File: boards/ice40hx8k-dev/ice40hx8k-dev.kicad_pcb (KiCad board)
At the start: 6 copper layers, 50 x 50 mm, 52 parts, among them U1 ICE40HX8K-CT256

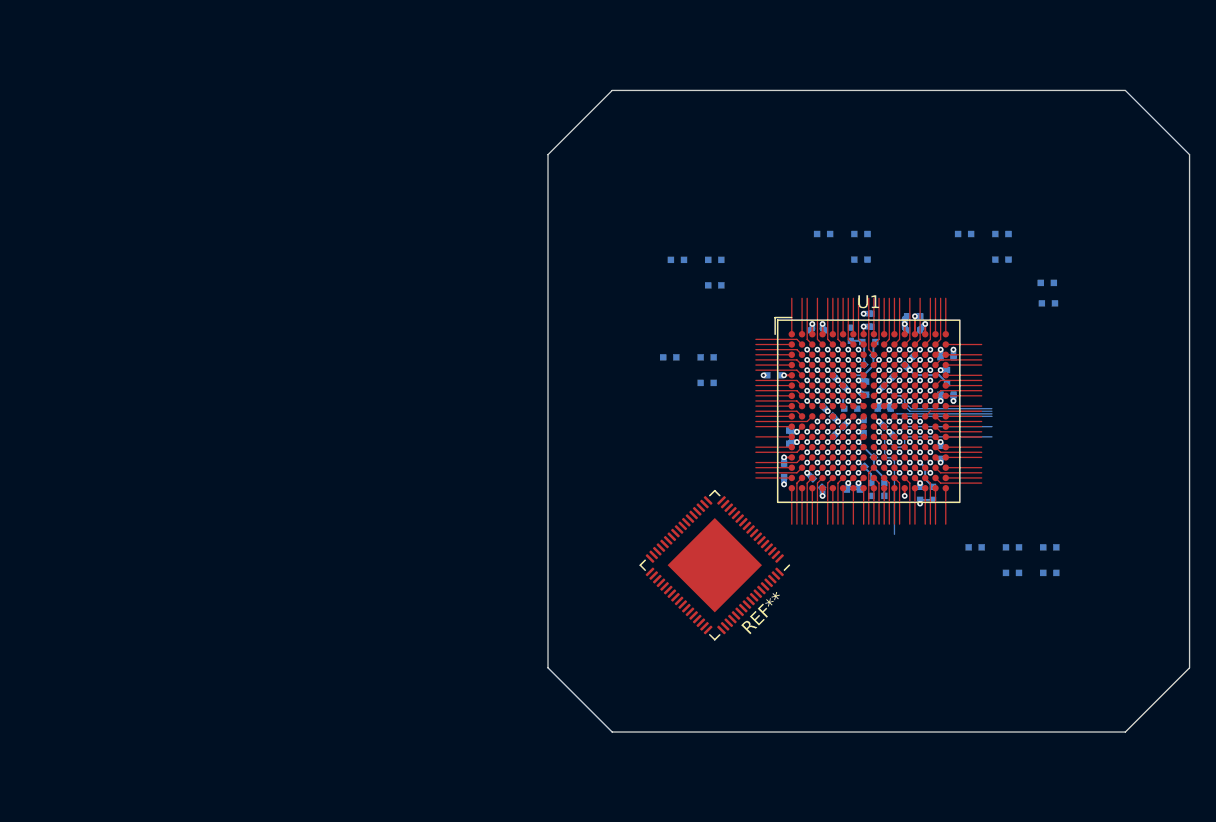
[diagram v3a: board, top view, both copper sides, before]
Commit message: Add USB connector and FT2323 symbol.
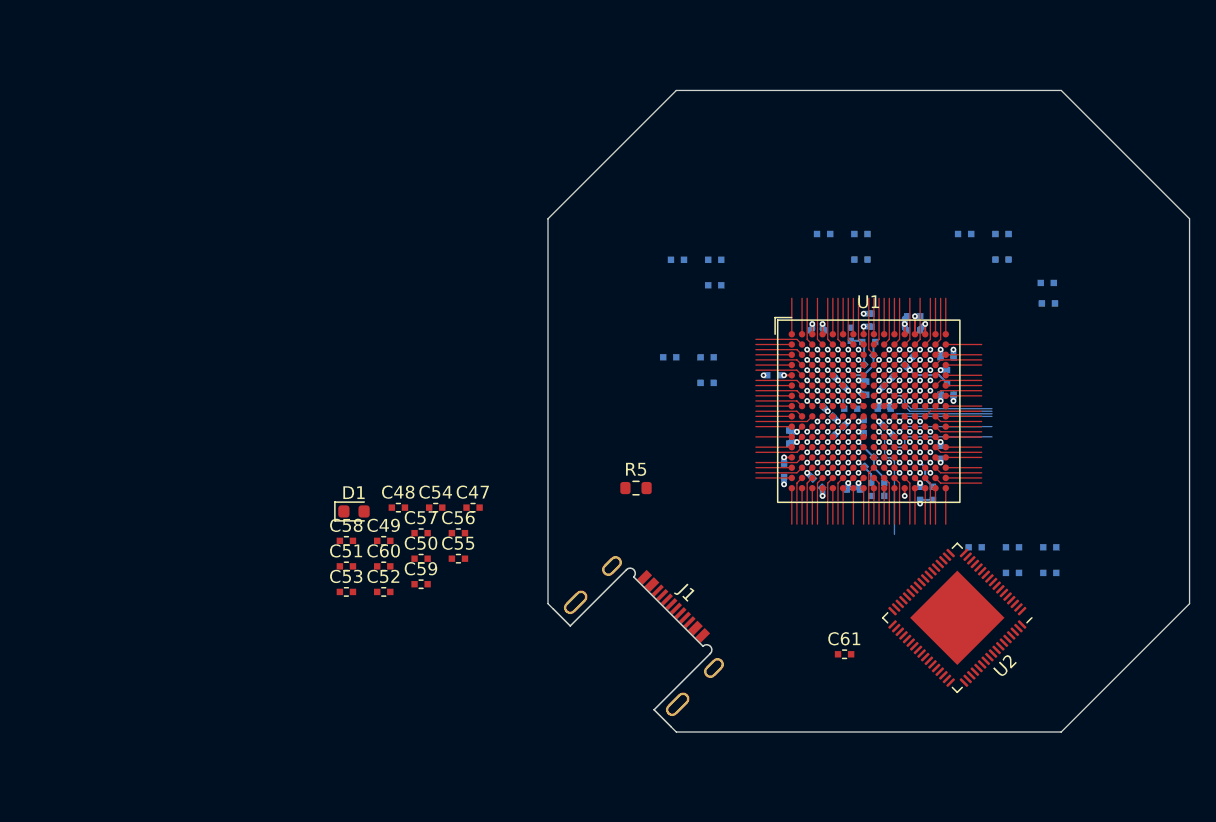
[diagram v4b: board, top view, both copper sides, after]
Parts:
- added C47: 10u, 0Local:C_SMD_0402_Pad0.5mm, F.Cu at (114.2, 102.5)
- added C48: 100n, 0Local:C_SMD_0402_Pad0.5mm, F.Cu at (108.3, 102.5)
- added C49: 100n, 0Local:C_SMD_0402_Pad0.5mm, F.Cu at (107.2, 105.1)
- added C50: 100n, 0Local:C_SMD_0402_Pad0.5mm, F.Cu at (110.1, 106.5)
- added C51: 100n, 0Local:C_SMD_0402_Pad0.5mm, F.Cu at (104.3, 107.1)
- added C52: 100n, 0Local:C_SMD_0402_Pad0.5mm, F.Cu at (107.2, 109.1)
- added C53: 100n, 0Local:C_SMD_0402_Pad0.5mm, F.Cu at (104.3, 109.1)
- added C54: 100n, 0Local:C_SMD_0402_Pad0.5mm, F.Cu at (111.2, 102.5)
- added C55: 100n, 0Local:C_SMD_0402_Pad0.5mm, F.Cu at (113.0, 106.5)
- added C56: 100n, 0Local:C_SMD_0402_Pad0.5mm, F.Cu at (113.0, 104.5)
- added C57: 100n, 0Local:C_SMD_0402_Pad0.5mm, F.Cu at (110.1, 104.5)
- added C58: 100n, 0Local:C_SMD_0402_Pad0.5mm, F.Cu at (104.3, 105.1)
- added C59: 100n, 0Local:C_SMD_0402_Pad0.5mm, F.Cu at (110.1, 108.5)
- added C60: 100n, 0Local:C_SMD_0402_Pad0.5mm, F.Cu at (107.2, 107.1)
- added C61: 100n, 0Local:C_SMD_0402_Pad0.5mm, F.Cu at (143.1, 113.9)
- added D1: D_Schottky, Diode_SMD:D_0603_1608Metric, F.Cu at (104.9, 102.8)
- added J1: USB4500-03-0-A, 0Local:GCT_USB4500, F.Cu at (126.9, 113.1)
- added R5: 12k, Resistor_SMD:R_0603_1608Metric, F.Cu at (126.9, 101.0)
- moved U2 19.3 mm to (151.9, 111.1)
- renumbered REF** to U2
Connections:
- U2 pad 1: (no net) -> unconnected-(U2-Pad1)
- U2 pad 10: (no net) -> +3V3
- U2 pad 11: (no net) -> /IO_Bank_2/ADBUS2
- U2 pad 12: (no net) -> /IO_Bank_2/ADBUS3
- U2 pad 13: (no net) -> /IO_Bank_2/ADBUS4
- U2 pad 14: (no net) -> /IO_Bank_2/ADBUS5
- U2 pad 15: (no net) -> /IO_Bank_2/ADBUS6
- U2 pad 16: (no net) -> /IO_Bank_2/ADBUS7
- U2 pad 17: (no net) -> /IO_Bank_2/ACBUS0
- U2 pad 18: (no net) -> /IO_Bank_2/ACBUS1
- U2 pad 19: (no net) -> /IO_Bank_2/ACBUS2
- U2 pad 2: (no net) -> unconnected-(U2-Pad2)
- U2 pad 20: (no net) -> /IO_Bank_2/ACBUS3
- U2 pad 21: (no net) -> /IO_Bank_2/ACBUS4
- U2 pad 22: (no net) -> /IO_Bank_2/ACBUS5
- U2 pad 23: (no net) -> /IO_Bank_2/ACBUS6
- U2 pad 24: (no net) -> /IO_Bank_2/ACBUS7
- U2 pad 25: (no net) -> Net-(U2-Pad25)
- U2 pad 26: (no net) -> +3V3
- U2 pad 27: (no net) -> unconnected-(U2-Pad27)
- U2 pad 28: (no net) -> unconnected-(U2-Pad28)
- U2 pad 29: (no net) -> GND
- U2 pad 3: (no net) -> GND
- U2 pad 30: (no net) -> Net-(U2-Pad30)
- U2 pad 31: (no net) -> Net-(U2-Pad25)
- U2 pad 32: (no net) -> unconnected-(U2-Pad32)
- U2 pad 33: (no net) -> unconnected-(U2-Pad33)
- U2 pad 34: (no net) -> /IO_Bank_2/BDBUS0
- U2 pad 35: (no net) -> /IO_Bank_2/BDBUS1
- U2 pad 36: (no net) -> /IO_Bank_2/BDBUS2
- U2 pad 37: (no net) -> /IO_Bank_2/BDBUS3
- U2 pad 38: (no net) -> /IO_Bank_2/BDBUS4
- U2 pad 39: (no net) -> +3V3
- U2 pad 4: (no net) -> unconnected-(U2-Pad4)
- U2 pad 40: (no net) -> /IO_Bank_2/BDBUS5
- U2 pad 41: (no net) -> /IO_Bank_2/BDBUS6
- U2 pad 42: (no net) -> /IO_Bank_2/BDBUS7
- U2 pad 43: (no net) -> unconnected-(U2-Pad43)
- U2 pad 44: (no net) -> Net-(U2-Pad25)
- U2 pad 45: (no net) -> /IO_Bank_2/BCBUS0
- U2 pad 46: (no net) -> /IO_Bank_2/BCBUS1
- U2 pad 47: (no net) -> /IO_Bank_2/BCBUS2
- U2 pad 48: (no net) -> /IO_Bank_2/BCBUS3
- U2 pad 49: (no net) -> /IO_Bank_2/BCBUS4
- U2 pad 5: (no net) -> unconnected-(U2-Pad5)
- U2 pad 50: (no net) -> /IO_Bank_2/BCBUS5
- U2 pad 51: (no net) -> +3V3
- U2 pad 52: (no net) -> /IO_Bank_2/BCBUS6
- U2 pad 53: (no net) -> /IO_Bank_2/BCBUS7
- U2 pad 54: (no net) -> unconnected-(U2-Pad54)
- U2 pad 55: (no net) -> unconnected-(U2-Pad55)
- U2 pad 56: (no net) -> unconnected-(U2-Pad56)
- U2 pad 57: (no net) -> Net-(U2-Pad57)
- U2 pad 58: (no net) -> /USB_Config/USB_D_N
- U2 pad 59: (no net) -> /USB_Config/USB_D_P
- U2 pad 6: (no net) -> /IO_Bank_2/ADBUS0
- U2 pad 60: (no net) -> Net-(R5-Pad1)
- U2 pad 61: (no net) -> Net-(U2-Pad61)
- U2 pad 62: (no net) -> /USB_Config/USB_CC2
- U2 pad 63: (no net) -> Net-(U2-Pad63)
- U2 pad 64: (no net) -> Net-(U2-Pad64)
- U2 pad 65: (no net) -> /USB_Config/USB_CC1
- U2 pad 66: (no net) -> Net-(U2-Pad25)
- U2 pad 67: (no net) -> unconnected-(U2-Pad67)
- U2 pad 68: (no net) -> unconnected-(U2-Pad68)
- U2 pad 7: (no net) -> /IO_Bank_2/ADBUS1
- U2 pad 8: (no net) -> Net-(U2-Pad25)
- U2 pad 9: (no net) -> GND
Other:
- outline, holes or cut-outs redrawn

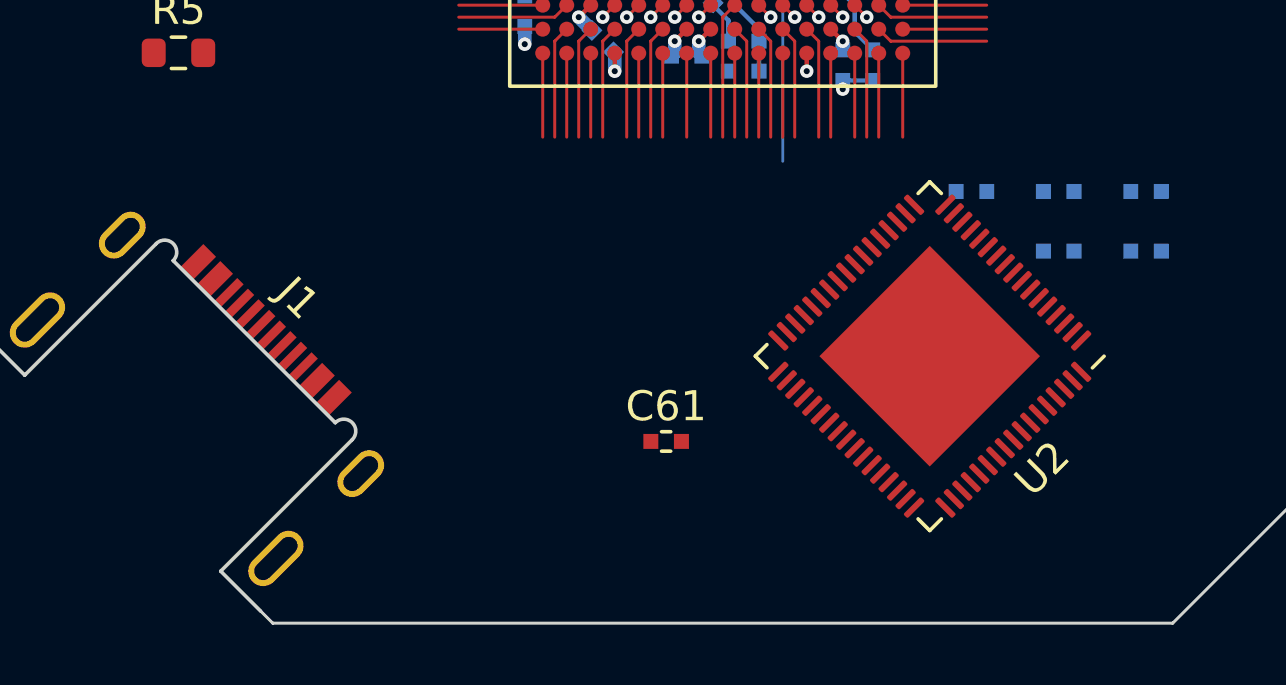
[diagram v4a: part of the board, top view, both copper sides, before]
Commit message: Use a lower-profile version of the USB connector.
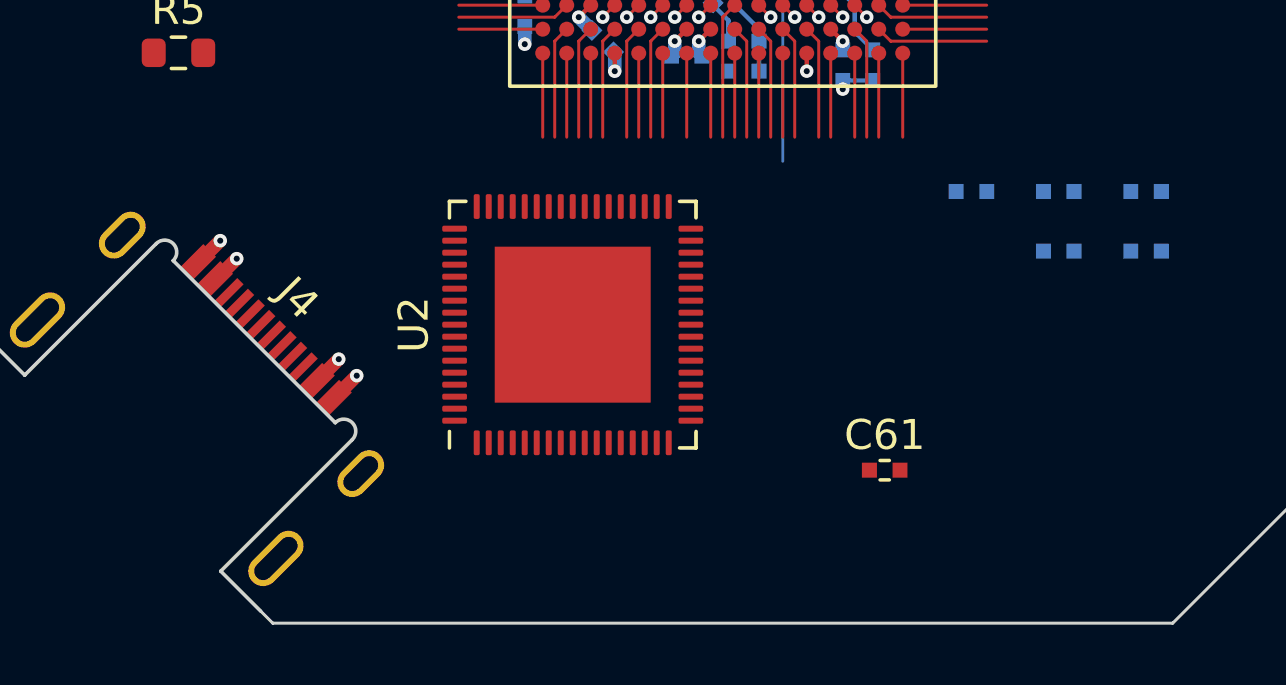
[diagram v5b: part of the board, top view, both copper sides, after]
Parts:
- J4: renamed from J1; value USB4500-03-0-A -> USB4520-03-1; footprint 0Local:GCT_USB4500 -> 0Local:GCT_USB45xx
- moved U2 11.9 mm to (140.0, 110.0), turned to 90 degrees
- moved C61 7.35 mm to (150.4, 114.9)
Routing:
- net GND: track 24.2 -> 26.3 mm, vias 26 -> 28
- net VBUS: track 0.00 -> 2.04 mm, vias 0 -> 2

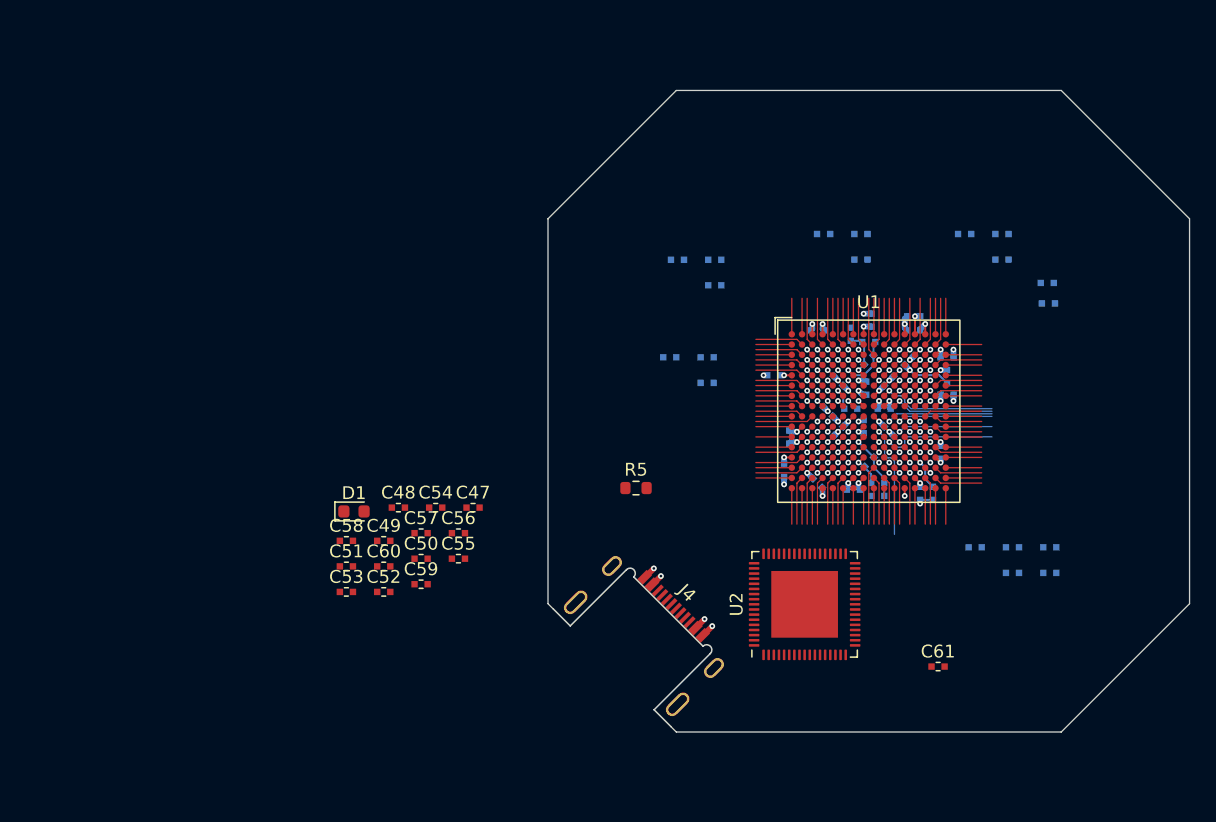
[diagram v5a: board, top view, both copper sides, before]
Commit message: Add Hirose connectors and standoffs.
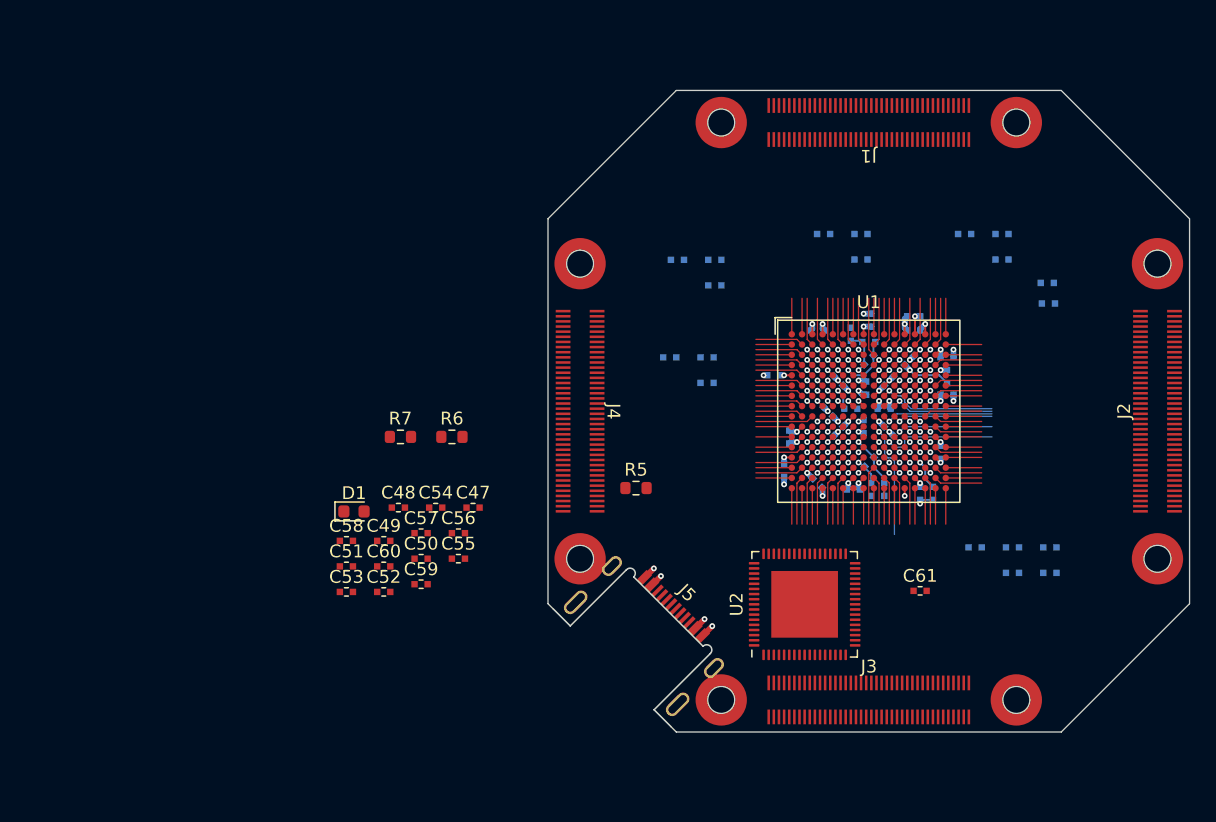
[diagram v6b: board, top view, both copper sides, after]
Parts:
- added H1: 9774020633, Mounting_Wuerth:Mounting_Wuerth_WA-SMSI-M1.6_H2mm_9774020633, F.Cu at (156.5, 72.5)
- added H2: 9774020633, Mounting_Wuerth:Mounting_Wuerth_WA-SMSI-M1.6_H2mm_9774020633, F.Cu at (133.5, 72.5)
- added H3: 9774020633, Mounting_Wuerth:Mounting_Wuerth_WA-SMSI-M1.6_H2mm_9774020633, F.Cu at (167.5, 106.5)
- added H4: 9774020633, Mounting_Wuerth:Mounting_Wuerth_WA-SMSI-M1.6_H2mm_9774020633, F.Cu at (167.5, 83.5)
- added H5: 9774020633, Mounting_Wuerth:Mounting_Wuerth_WA-SMSI-M1.6_H2mm_9774020633, F.Cu at (133.5, 117.5)
- added H6: 9774020633, Mounting_Wuerth:Mounting_Wuerth_WA-SMSI-M1.6_H2mm_9774020633, F.Cu at (156.5, 117.5)
- added H7: 9774020633, Mounting_Wuerth:Mounting_Wuerth_WA-SMSI-M1.6_H2mm_9774020633, F.Cu at (122.5, 83.5)
- added H8: 9774020633, Mounting_Wuerth:Mounting_Wuerth_WA-SMSI-M1.6_H2mm_9774020633, F.Cu at (122.5, 106.5)
- added J1: DF40HC(2.0)-80DS, 0Local:Hirose_DF40C-80DS, F.Cu at (145.0, 72.5)
- added J2: DF40HC(2.0)-80DS, 0Local:Hirose_DF40C-80DS, F.Cu at (167.5, 95.0)
- added J3: DF40HC(2.0)-80DS, 0Local:Hirose_DF40C-80DS, F.Cu at (145.0, 117.5)
- added J4: DF40HC(2.0)-80DS, 0Local:Hirose_DF40C-80DS, F.Cu at (122.5, 95.0)
- added R6: 100k, Resistor_SMD:R_0603_1608Metric, F.Cu at (112.5, 97.0)
- added R7: 15k, Resistor_SMD:R_0603_1608Metric, F.Cu at (108.5, 97.0)
- moved C61 6.06 mm to (149.0, 109.0)
- renumbered J4 to J5

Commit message: Switch to 4mm Hirose connectors and different mounting holes.
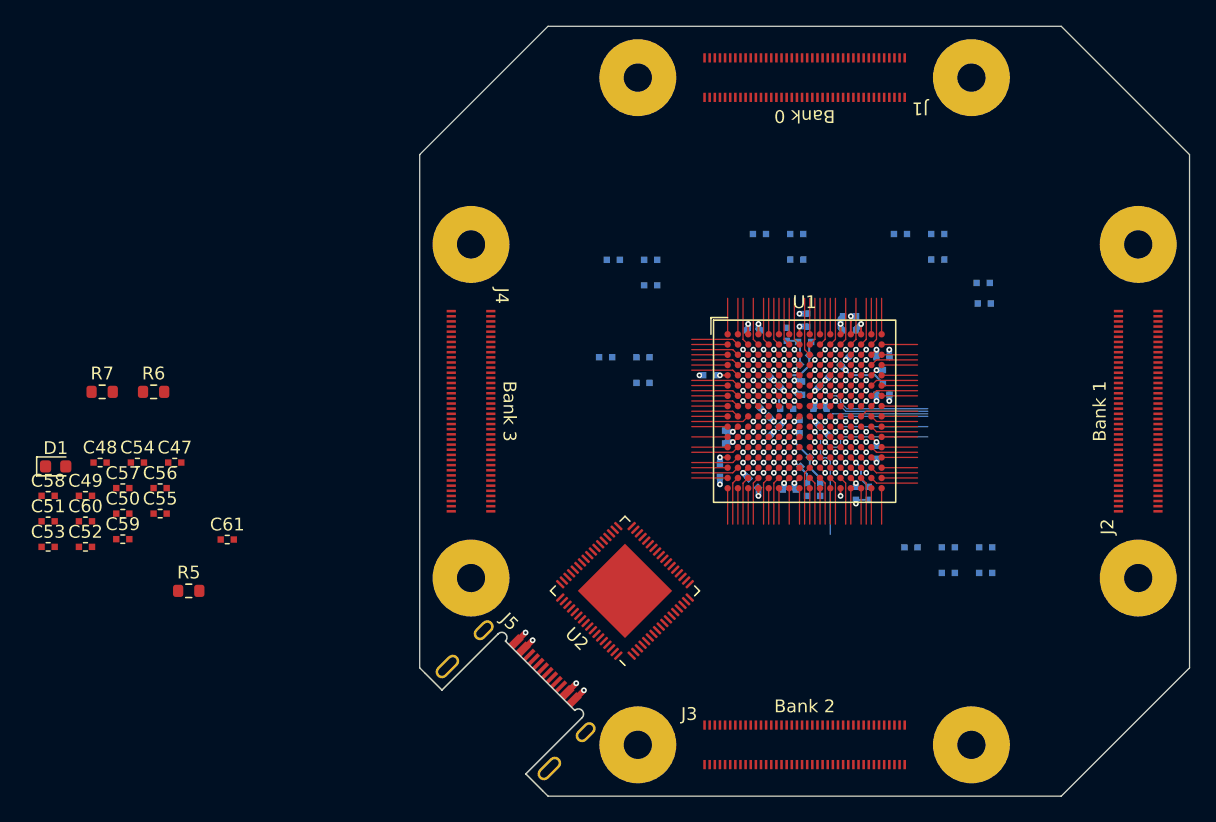
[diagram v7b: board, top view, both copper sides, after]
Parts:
- H1, H2, H3, H4, H5, H6, H7, H8: footprint Mounting_Wuerth:Mounting_Wuerth_WA-SMSI-M1.6_H2mm_9774020633 -> 0Local:MountingHole_2.2mm_M2_Pad6mm
- J1, J2, J3, J4: value DF40HC(2.0)-80DS -> DF40HC(4.0)-80DS
- moved C61 54.1 mm to (95.0, 105.0)
- moved R5 35.8 mm to (92.0, 109.0)
- moved C47 23.5 mm to (90.9, 99.0)
- moved C50 23.5 mm to (86.9, 103.0)
- moved C54 23.5 mm to (88.0, 99.0)
- moved C55 23.5 mm to (89.8, 103.0)
- moved C56 23.5 mm to (89.8, 101.0)
- moved C57 23.5 mm to (86.9, 101.0)
- moved C59 23.5 mm to (86.9, 105.0)
- moved D1 23.5 mm to (81.6, 99.3)
- moved R6 23.5 mm to (89.3, 93.5)
- moved R7 23.5 mm to (85.3, 93.5)
- moved C48 23.5 mm to (85.1, 99.0)
- moved C49 23.5 mm to (84.0, 101.6)
- moved C51 23.5 mm to (81.0, 103.6)
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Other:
- board size 50 x 50 mm -> 60 x 60 mm
- board text added: "Bank 0"
- board text added: "Bank 1"
- board text added: "Bank 2"
- board text added: "Bank 3"
